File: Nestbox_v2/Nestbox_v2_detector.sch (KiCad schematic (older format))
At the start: 12 parts, among them P501 CONN_01X02, P502 CONN_01X02, U501 TSOP38, U502 TSOP38

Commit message: added PIR and lightbarrier headers
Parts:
- removed C501, C502: 1u, symbol C
- removed D501, D502: OSRAM_SFH4656, symbol OSRAM_SFH4656
- removed P501, P502: CONN_01X02, symbol CONN_01X02
- removed R501, R503: 100E, symbol R
- removed R502, R504: R, symbol R
- removed U501, U502: TSOP38, symbol TSOP38
- added J401, J402, J403: CONN_01X04, symbol CONN_01X04
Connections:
- net labels added: PIR_EN, PIR_OUT
- net labels removed: LB2_LED
- wire segments 26 -> 11
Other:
- note added: "INTERNAL\nEXTERNAL\n"
- note added: "TODO: CHECK IF TSALxxxx COMPONENT \nREQUIRES FILTERING OR BYPASS CAP OR SERIES RESISTOR\n"
- note removed: "TODO: add PIR motion sensor (results to be confirmed by Jiacheng"
- note removed: "currently testing SFH4941 as alternative…"
- note removed: "one emitting led probably enough\n"

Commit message: added power footprints, final connector footprints
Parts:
- J401, J402, J403: footprint (none) -> Terminal_Blocks:TerminalBlock_Pheonix_PT-3.5mm_4pol
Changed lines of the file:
@@
 $EndDescr
 $Comp
-L +3.3V #PWR038
+L +3.3V #PWR039
 U 1 1 59FD02D9
 P 2750 2200
-F 0 "#PWR038" H 2750 2050 50  0001 C CNN
+F 0 "#PWR039" H 2750 2050 50  0001 C CNN
 F 1 "+3.3V" V 2765 2328 50  0000 L CNN
 F 2 "" H 2750 2200 50  0000 C CNN
@@
 $EndComp
 $Comp
-L GND #PWR039
+L GND #PWR040
 U 1 1 59FD0355
 P 2750 2500
-F 0 "#PWR039" H 2750 2250 50  0001 C CNN
+F 0 "#PWR040" H 2750 2250 50  0001 C CNN
 F 1 "GND" V 2755 2372 50  0000 R CNN
 F 2 "" H 2750 2500 50  0000 C CNN
@@
 F 0 "J401" H 3100 2600 50  0000 C CNN
 F 1 "CONN_01X04" V 3200 2350 50  0000 C CNN
-F 2 "" H 3100 2350 50  0001 C CNN
+F 2 "Terminal_Blocks:TerminalBlock_Pheonix_PT-3.5mm_4pol" H 3100 2350 50  0001 C CNN
 F 3 "" H 3100 2350 50  0001 C CNN
 	1    3100 2350
@@
 F 0 "J403" H 5300 2600 50  0000 C CNN
 F 1 "CONN_01X04" V 5400 2350 50  0000 C CNN
-F 2 "" H 5300 2350 50  0001 C CNN
+F 2 "Terminal_Blocks:TerminalBlock_Pheonix_PT-3.5mm_4pol" H 5300 2350 50  0001 C CNN
 F 3 "" H 5300 2350 50  0001 C CNN
 	1    5300 2350
@@
 	4850 2300 5100 2300
 $Comp
-L +3.3V #PWR040
+L +3.3V #PWR041
 U 1 1 5B0A4946
 P 4850 2200
-F 0 "#PWR040" H 4850 2050 50  0001 C CNN
+F 0 "#PWR041" H 4850 2050 50  0001 C CNN
 F 1 "+3.3V" V 4865 2328 50  0000 L CNN
 F 2 "" H 4850 2200 50  0000 C CNN
@@
 	5100 2200 4850 2200
 $Comp
-L GND #PWR041
+L GND #PWR042
 U 1 1 5B0A49E1
 P 4850 2500
-F 0 "#PWR041" H 4850 2250 50  0001 C CNN
+F 0 "#PWR042" H 4850 2250 50  0001 C CNN
 F 1 "GND" V 4855 2372 50  0000 R CNN
 F 2 "" H 4850 2500 50  0000 C CNN
@@
 F 0 "J402" H 3100 3650 50  0000 C CNN
 F 1 "CONN_01X04" V 3200 3400 50  0000 C CNN
-F 2 "" H 3100 3400 50  0001 C CNN
+F 2 "Terminal_Blocks:TerminalBlock_Pheonix_PT-3.5mm_4pol" H 3100 3400 50  0001 C CNN
 F 3 "" H 3100 3400 50  0001 C CNN
 	1    3100 3400
@@
 $EndComp
 $Comp
-L GND #PWR042
+L GND #PWR043
 U 1 1 5B0B21F9
 P 2900 3550
-F 0 "#PWR042" H 2900 3300 50  0001 C CNN
+F 0 "#PWR043" H 2900 3300 50  0001 C CNN
 F 1 "GND" V 2905 3422 50  0000 R CNN
 F 2 "" H 2900 3550 50  0000 C CNN
@@
 $EndComp
 $Comp
-L +3.3V #PWR043
+L +3.3V #PWR044
 U 1 1 5B0B220D
 P 2900 3250
-F 0 "#PWR043" H 2900 3100 50  0001 C CNN
+F 0 "#PWR044" H 2900 3100 50  0001 C CNN
 F 1 "+3.3V" V 2915 3378 50  0000 L CNN
 F 2 "" H 2900 3250 50  0000 C CNN

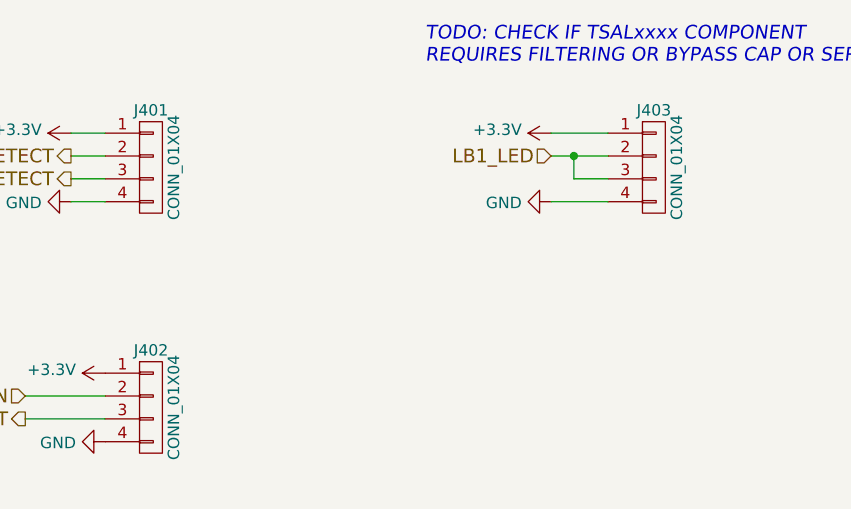
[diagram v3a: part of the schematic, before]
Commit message: correct size of the PCB drawn with connector arrangement done as well
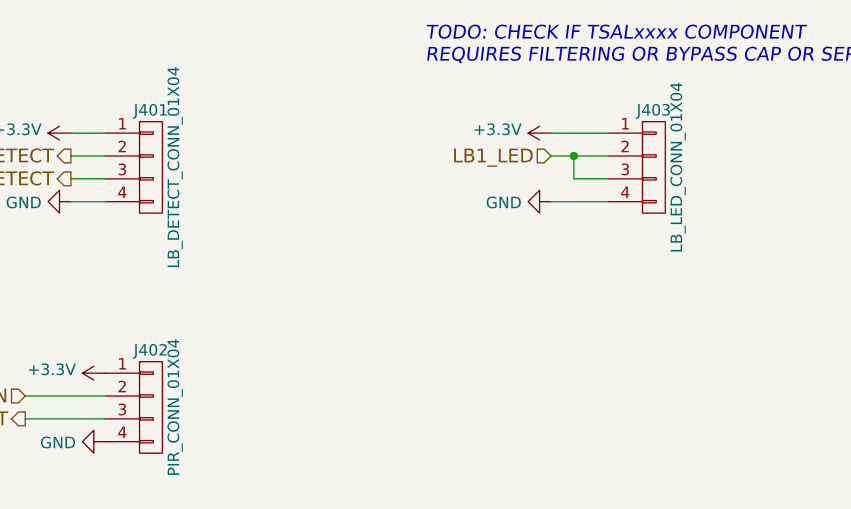
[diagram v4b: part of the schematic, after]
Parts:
- J401: value CONN_01X04 -> LB_DETECT_CONN_01X04
- J402: value CONN_01X04 -> PIR_CONN_01X04
- J403: value CONN_01X04 -> LB_LED_CONN_01X04
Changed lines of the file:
@@
 $EndDescr
 $Comp
-L +3.3V #PWR039
+L +3.3V #PWR401
 U 1 1 59FD02D9
 P 2750 2200
-F 0 "#PWR039" H 2750 2050 50  0001 C CNN
+F 0 "#PWR401" H 2750 2050 50  0001 C CNN
 F 1 "+3.3V" V 2765 2328 50  0000 L CNN
 F 2 "" H 2750 2200 50  0000 C CNN
@@
 $EndComp
 $Comp
-L GND #PWR040
+L GND #PWR402
 U 1 1 59FD0355
 P 2750 2500
-F 0 "#PWR040" H 2750 2250 50  0001 C CNN
+F 0 "#PWR402" H 2750 2250 50  0001 C CNN
 F 1 "GND" V 2755 2372 50  0000 R CNN
 F 2 "" H 2750 2500 50  0000 C CNN
@@
 P 3100 2350
 F 0 "J401" H 3100 2600 50  0000 C CNN
-F 1 "CONN_01X04" V 3200 2350 50  0000 C CNN
+F 1 "LB_DETECT_CONN_01X04" V 3200 2350 50  0000 C CNN
 F 2 "Terminal_Blocks:TerminalBlock_Pheonix_PT-3.5mm_4pol" H 3100 2350 50  0001 C CNN
 F 3 "" H 3100 2350 50  0001 C CNN
@@
 P 5300 2350
 F 0 "J403" H 5300 2600 50  0000 C CNN
-F 1 "CONN_01X04" V 5400 2350 50  0000 C CNN
+F 1 "LB_LED_CONN_01X04" V 5400 2350 50  0000 C CNN
 F 2 "Terminal_Blocks:TerminalBlock_Pheonix_PT-3.5mm_4pol" H 5300 2350 50  0001 C CNN
 F 3 "" H 5300 2350 50  0001 C CNN
@@
 	4850 2300 5100 2300
 $Comp
-L +3.3V #PWR041
+L +3.3V #PWR405
 U 1 1 5B0A4946
 P 4850 2200
-F 0 "#PWR041" H 4850 2050 50  0001 C CNN
+F 0 "#PWR405" H 4850 2050 50  0001 C CNN
 F 1 "+3.3V" V 4865 2328 50  0000 L CNN
 F 2 "" H 4850 2200 50  0000 C CNN
@@
 	5100 2200 4850 2200
 $Comp
-L GND #PWR042
+L GND #PWR406
 U 1 1 5B0A49E1
 P 4850 2500
-F 0 "#PWR042" H 4850 2250 50  0001 C CNN
+F 0 "#PWR406" H 4850 2250 50  0001 C CNN
 F 1 "GND" V 4855 2372 50  0000 R CNN
 F 2 "" H 4850 2500 50  0000 C CNN
@@
 P 3100 3400
 F 0 "J402" H 3100 3650 50  0000 C CNN
-F 1 "CONN_01X04" V 3200 3400 50  0000 C CNN
+F 1 "PIR_CONN_01X04" V 3200 3400 50  0000 C CNN
 F 2 "Terminal_Blocks:TerminalBlock_Pheonix_PT-3.5mm_4pol" H 3100 3400 50  0001 C CNN
 F 3 "" H 3100 3400 50  0001 C CNN
@@
 $EndComp
 $Comp
-L GND #PWR043
+L GND #PWR404
 U 1 1 5B0B21F9
 P 2900 3550
-F 0 "#PWR043" H 2900 3300 50  0001 C CNN
+F 0 "#PWR404" H 2900 3300 50  0001 C CNN
 F 1 "GND" V 2905 3422 50  0000 R CNN
 F 2 "" H 2900 3550 50  0000 C CNN
@@
 $EndComp
 $Comp
-L +3.3V #PWR044
+L +3.3V #PWR403
 U 1 1 5B0B220D
 P 2900 3250
-F 0 "#PWR044" H 2900 3100 50  0001 C CNN
+F 0 "#PWR403" H 2900 3100 50  0001 C CNN
 F 1 "+3.3V" V 2915 3378 50  0000 L CNN
 F 2 "" H 2900 3250 50  0000 C CNN

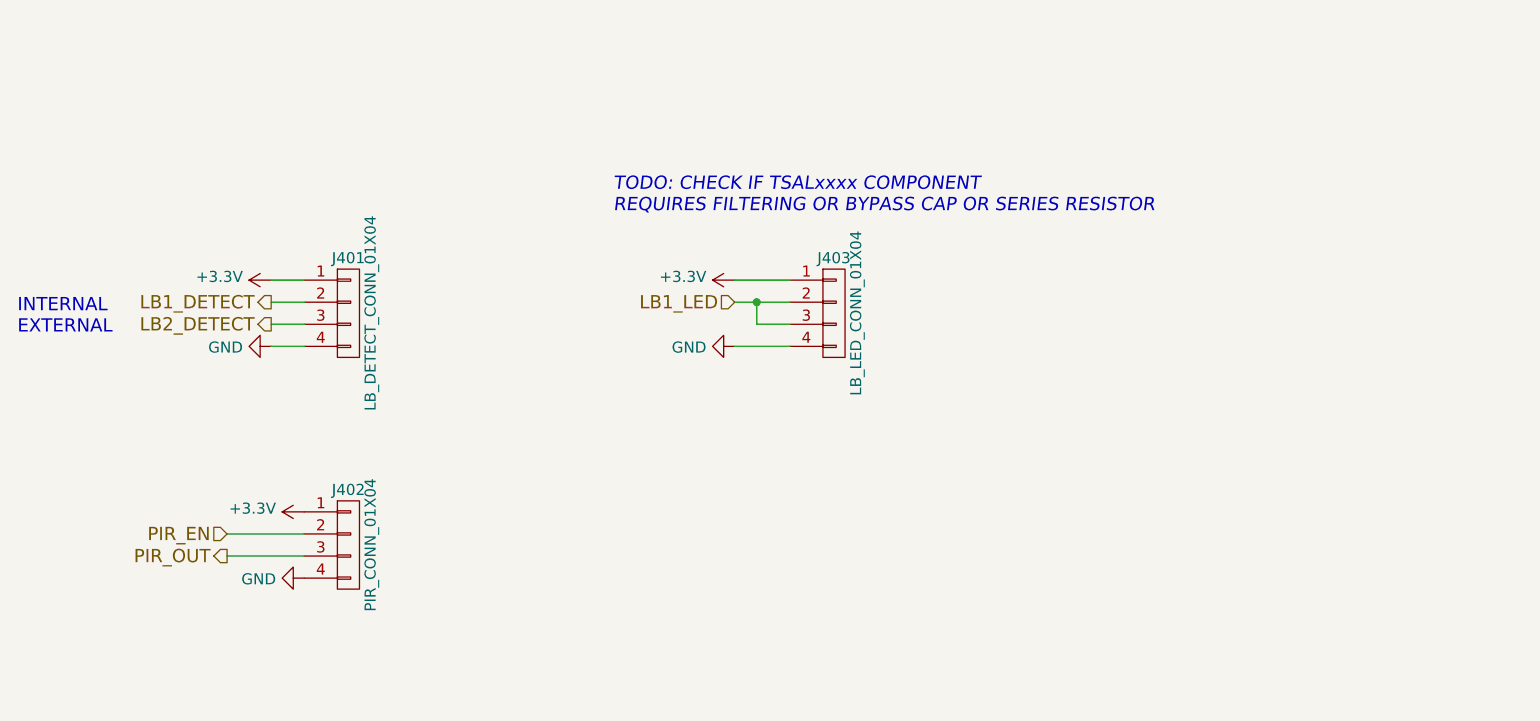
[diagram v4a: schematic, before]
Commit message: all footprints assigned except mosfets; final connectors and their locatino, started component placement
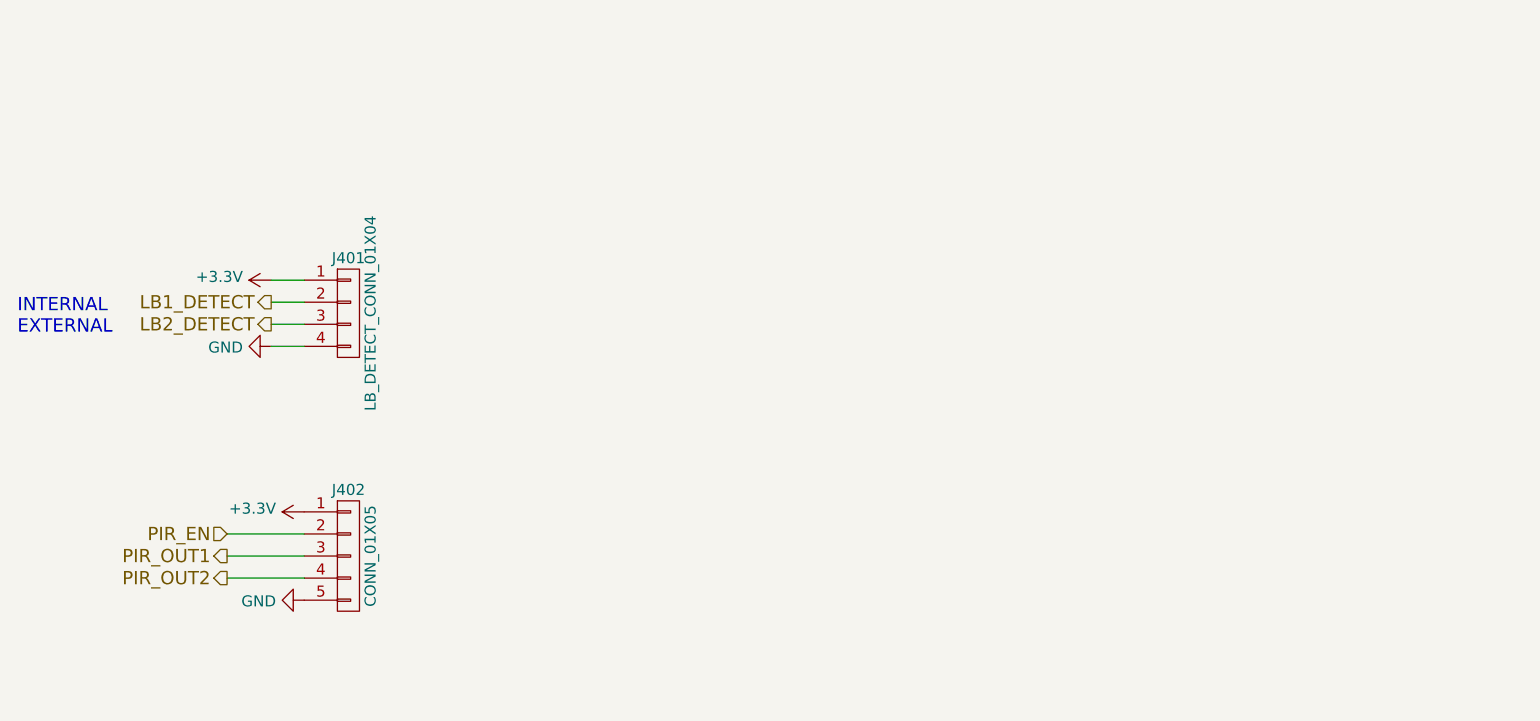
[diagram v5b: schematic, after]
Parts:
- removed J402: PIR_CONN_01X04, Terminal_Blocks:TerminalBlock_Pheonix_PT-3.5mm_4pol, symbol CONN_01X04
- removed J403: LB_LED_CONN_01X04, Terminal_Blocks:TerminalBlock_Pheonix_PT-3.5mm_4pol, symbol CONN_01X04
- added J402: CONN_01X05, Terminal_Blocks:TerminalBlock_Pheonix_MPT-2.54mm_5pol, symbol CONN_01X05
- J401: footprint Terminal_Blocks:TerminalBlock_Pheonix_PT-3.5mm_4pol -> Terminal_Blocks:TerminalBlock_Pheonix_MPT-2.54mm_4pol
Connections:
- net +3V3: now also J402.1 (P1)
- net GND: now also J402.5 (P5)
- net PIR_EN: now also J402.2 (P2)
- new net PIR_OUT1: J402.3 (P3)
- new net PIR_OUT2: J402.4 (P4)
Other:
- note removed: "TODO: CHECK IF TSALxxxx COMPONENT \nREQUIRES FILTERING OR BYPASS CAP OR SERIES RESISTOR\n"
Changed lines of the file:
@@
 EESchema Schematic File Version 2
-LIBS:Nestbox_v2-rescue
-LIBS:Octanis3
 LIBS:power
 LIBS:device
-LIBS:switches
-LIBS:relays
-LIBS:motors
 LIBS:transistors
 LIBS:conn
@@
 LIBS:contrib
 LIBS:valves
-LIBS:SeeedOPL-Capacitor-2016
-LIBS:SeeedOPL-Connector-2016
-LIBS:SeeedOPL-Crystal Oscillator-2016
-LIBS:SeeedOPL-Diode-2016
-LIBS:SeeedOPL-Display-2016
-LIBS:SeeedOPL-Fuse-2016
-LIBS:SeeedOPL-IC-2016
-LIBS:SeeedOPL-Inductor-2016
-LIBS:SeeedOPL-LED-2016
-LIBS:SeeedOPL-Relay-2016
-LIBS:SeeedOPL-Resistor-2016
-LIBS:SeeedOPL-Sensor-2016
-LIBS:SeeedOPL-Switch-2016
-LIBS:SeeedOPL-Transistor-2016
+LIBS:Octanis3
 LIBS:Nestbox_v2-cache
 EELAYER 25 0
@@
 $EndDescr
 $Comp
-L +3.3V #PWR401
+L +3.3V #PWR042
 U 1 1 59FD02D9
 P 2750 2200
-F 0 "#PWR401" H 2750 2050 50  0001 C CNN
+F 0 "#PWR042" H 2750 2050 50  0001 C CNN
 F 1 "+3.3V" V 2765 2328 50  0000 L CNN
 F 2 "" H 2750 2200 50  0000 C CNN
@@
 $EndComp
 $Comp
-L GND #PWR402
+L GND #PWR043
 U 1 1 59FD0355
 P 2750 2500
-F 0 "#PWR402" H 2750 2250 50  0001 C CNN
+F 0 "#PWR043" H 2750 2250 50  0001 C CNN
 F 1 "GND" V 2755 2372 50  0000 R CNN
 F 2 "" H 2750 2500 50  0000 C CNN
@@
 	0    1    1    0
 $EndComp
-Text Notes 4300 1900 0    60   Italic 0
-TODO: CHECK IF TSALxxxx COMPONENT \nREQUIRES FILTERING OR BYPASS CAP OR SERIES RESISTOR\n
 $Comp
 L CONN_01X04 J401
@@
 F 0 "J401" H 3100 2600 50  0000 C CNN
 F 1 "LB_DETECT_CONN_01X04" V 3200 2350 50  0000 C CNN
-F 2 "Terminal_Blocks:TerminalBlock_Pheonix_PT-3.5mm_4pol" H 3100 2350 50  0001 C CNN
+F 2 "Terminal_Blocks:TerminalBlock_Pheonix_MPT-2.54mm_4pol" H 3100 2350 50  0001 C CNN
 F 3 "" H 3100 2350 50  0001 C CNN
 	1    3100 2350
@@
 Wire Wire Line
 	2750 2500 2900 2500
-Text HLabel 4850 2300 0    60   Input ~ 0
-LB1_LED
-$Comp
-L CONN_01X04 J403
-U 1 1 5B0A4868
-P 5300 2350
-F 0 "J403" H 5300 2600 50  0000 C CNN
-F 1 "LB_LED_CONN_01X04" V 5400 2350 50  0000 C CNN
-F 2 "Terminal_Blocks:TerminalBlock_Pheonix_PT-3.5mm_4pol" H 5300 2350 50  0001 C CNN
-F 3 "" H 5300 2350 50  0001 C CNN
-	1    5300 2350
-	1    0    0    -1
-$EndComp
-Wire Wire Line
-	4850 2300 5100 2300
-$Comp
-L +3.3V #PWR405
-U 1 1 5B0A4946
-P 4850 2200
-F 0 "#PWR405" H 4850 2050 50  0001 C CNN
-F 1 "+3.3V" V 4865 2328 50  0000 L CNN
-F 2 "" H 4850 2200 50  0000 C CNN
-F 3 "" H 4850 2200 50  0000 C CNN
-	1    4850 2200
-	0    -1   -1   0
-$EndComp
-Wire Wire Line
-	5100 2200 4850 2200
-$Comp
-L GND #PWR406
-U 1 1 5B0A49E1
-P 4850 2500
-F 0 "#PWR406" H 4850 2250 50  0001 C CNN
-F 1 "GND" V 4855 2372 50  0000 R CNN
-F 2 "" H 4850 2500 50  0000 C CNN
-F 3 "" H 4850 2500 50  0000 C CNN
-	1    4850 2500
-	0    1    1    0
-$EndComp
-Wire Wire Line
-	4850 2500 5100 2500
-Wire Wire Line
-	5100 2400 4950 2400
-Wire Wire Line
-	4950 2400 4950 2300
-Connection ~ 4950 2300
 Text Notes 1600 2450 0    60   ~ 0
 INTERNAL\nEXTERNAL\n
 $Comp
-L CONN_01X04 J402
-U 1 1 5B0B21DB
-P 3100 3400
-F 0 "J402" H 3100 3650 50  0000 C CNN
-F 1 "PIR_CONN_01X04" V 3200 3400 50  0000 C CNN
-F 2 "Terminal_Blocks:TerminalBlock_Pheonix_PT-3.5mm_4pol" H 3100 3400 50  0001 C CNN
-F 3 "" H 3100 3400 50  0001 C CNN
-	1    3100 3400
-	1    0    0    -1
-$EndComp
-$Comp
-L GND #PWR404
+L GND #PWR044
 U 1 1 5B0B21F9
-P 2900 3550
-F 0 "#PWR404" H 2900 3300 50  0001 C CNN
-F 1 "GND" V 2905 3422 50  0000 R CNN
-F 2 "" H 2900 3550 50  0000 C CNN
-F 3 "" H 2900 3550 50  0000 C CNN
-	1    2900 3550
+P 2900 3650
+F 0 "#PWR044" H 2900 3400 50  0001 C CNN
+F 1 "GND" V 2905 3522 50  0000 R CNN
+F 2 "" H 2900 3650 50  0000 C CNN
+F 3 "" H 2900 3650 50  0000 C CNN
+	1    2900 3650
 	0    1    1    0
 $EndComp
 $Comp
-L +3.3V #PWR403
+L +3.3V #PWR045
 U 1 1 5B0B220D
 P 2900 3250
-F 0 "#PWR403" H 2900 3100 50  0001 C CNN
+F 0 "#PWR045" H 2900 3100 50  0001 C CNN
 F 1 "+3.3V" V 2915 3378 50  0000 L CNN
 F 2 "" H 2900 3250 50  0000 C CNN
@@
 PIR_EN
 Text HLabel 2550 3450 0    60   Output ~ 0
-PIR_OUT
+PIR_OUT1
+Text HLabel 2550 3550 0    60   Output ~ 0
+PIR_OUT2
+$Comp
+L CONN_01X05 J402
+U 1 1 5B1512A0
+P 3100 3450
+F 0 "J402" H 3100 3750 50  0000 C CNN
+F 1 "CONN_01X05" V 3200 3450 50  0000 C CNN
+F 2 "Terminal_Blocks:TerminalBlock_Pheonix_MPT-2.54mm_5pol" H 3100 3450 50  0001 C CNN
+F 3 "" H 3100 3450 50  0001 C CNN
+	1    3100 3450
+	1    0    0    -1
+$EndComp
+Wire Wire Line
+	2900 3550 2550 3550
 $EndSCHEMATC
